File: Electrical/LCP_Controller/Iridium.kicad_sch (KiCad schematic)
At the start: 5 parts, among them J13 SALEAE_TEST, J14 U.FL, U14 IRIDIUM_9603N

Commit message: Hardware Revision : v0.3
1. modified schematic design, removed unnecessary test points.
2. pcb layout 2x8 Inches allowance dimension, layout is in progress
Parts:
- removed TP54: 5000, TestPoint:TestPoint_Keystone_5000-5004_Miniature, symbol Connector:TestPoint
- removed TP55: 5001, TestPoint:TestPoint_Keystone_5000-5004_Miniature, symbol Connector:TestPoint
- renumbered J13 to J5, J14 to J6, U14 to U5
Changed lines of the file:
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@@
-    (stroke (width 0) (type default) (color 0 0 0 0))
-  )
-  (wire (pts (xy 187.96 83.82) (xy 187.96 85.09))
     (stroke (width 0) (type default) (color 0 0 0 0))
   )
@@
   )
   (wire (pts (xy 161.29 123.19) (xy 161.29 125.73))
-    (stroke (width 0) (type default) (color 0 0 0 0))
-  )
-  (wire (pts (xy 163.83 83.82) (xy 163.83 86.36))
     (stroke (width 0) (type default) (color 0 0 0 0))
   )
@@
     (effects (font (size 1.27 1.27)) (justify right))
   )
-  (symbol (lib_id "Connector:TestPoint") (at 163.83 83.82 0) (unit 1)
-    (in_bom yes) (on_board yes)
-    (property "Reference" "TP54" (id 0) (at 165.3032 79.6798 0)
-      (effects (font (size 1.27 1.27)) (justify left))
-    )
-    (property "Value" "5000" (id 1) (at 165.3032 81.9912 0)
-      (effects (font (size 1.27 1.27)) (justify left))
-    )
-    (property "Footprint" "TestPoint:TestPoint_Keystone_5000-5004_Miniature" (id 2) (at 168.91 83.82 0)
-      (effects (font (size 1.27 1.27)) hide)
-    )
-    (property "Datasheet" "~" (id 3) (at 168.91 83.82 0)
-      (effects (font (size 1.27 1.27)) hide)
-    )
-    (property "TestPoint" "EXT_PWR" (id 4) (at 165.3032 84.3026 0)
-      (effects (font (size 1.27 1.27)) (justify left) hide)
-    )
-    (property "MPN" "" (id 5) (at 163.83 83.82 0)
-      (effects (font (size 1.27 1.27)) hide)
-    )
-    (pin "1")
-  )
-  (symbol (lib_id "Connector:TestPoint") (at 187.96 83.82 0) (unit 1)
-    (in_bom yes) (on_board yes)
-    (property "Reference" "TP55" (id 0) (at 189.4332 80.8228 0)
-      (effects (font (size 1.27 1.27)) (justify left))
-    )
-    (property "Value" "5001" (id 1) (at 189.4332 83.1342 0)
-      (effects (font (size 1.27 1.27)) (justify left))
-    )
-    (property "Footprint" "TestPoint:TestPoint_Keystone_5000-5004_Miniature" (id 2) (at 193.04 83.82 0)
-      (effects (font (size 1.27 1.27)) hide)
-    )
-    (property "Datasheet" "~" (id 3) (at 193.04 83.82 0)
-      (effects (font (size 1.27 1.27)) hide)
-    )
-    (property "TestPoint" "GND" (id 4) (at 187.96 83.82 0)
-      (effects (font (size 1.27 1.27)) hide)
-    )
-    (property "MPN" "" (id 5) (at 187.96 83.82 0)
-      (effects (font (size 1.27 1.27)) hide)
-    )
-    (pin "1")
-  )
-  (symbol (lib_id "power:GND") (at 187.96 85.09 0) (unit 1)
-    (in_bom yes) (on_board yes)
-    (property "Reference" "#PWR0125" (id 0) (at 187.96 91.44 0)
-      (effects (font (size 1.27 1.27)) hide)
-    )
-    (property "Value" "GND" (id 1) (at 188.087 89.4842 0))
-    (property "Footprint" "" (id 2) (at 187.96 85.09 0)
-      (effects (font (size 1.27 1.27)) hide)
-    )
-    (property "Datasheet" "" (id 3) (at 187.96 85.09 0)
-      (effects (font (size 1.27 1.27)) hide)
-    )
-    (pin "1")
-  )
   (symbol (lib_id "power:GND") (at 166.37 127 0) (unit 1)
     (in_bom yes) (on_board yes)
-    (property "Reference" "#PWR081" (id 0) (at 166.37 133.35 0)
+    (property "Reference" "#PWR047" (id 0) (at 166.37 133.35 0)
       (effects (font (size 1.27 1.27)) hide)
     )
@@
   (symbol (lib_id "Connector_Generic:Conn_02x04_Odd_Even") (at 129.54 81.28 90) (unit 1)
     (in_bom yes) (on_board yes)
-    (property "Reference" "J13" (id 0) (at 137.16 77.47 90)
+    (property "Reference" "J5" (id 0) (at 137.16 77.47 90)
       (effects (font (size 1.27 1.27)) (justify right))
     )
@@
   (symbol (lib_id "power:GND") (at 119.38 77.47 0) (unit 1)
     (in_bom yes) (on_board yes)
-    (property "Reference" "#PWR079" (id 0) (at 119.38 83.82 0)
+    (property "Reference" "#PWR044" (id 0) (at 119.38 83.82 0)
       (effects (font (size 1.27 1.27)) hide)
     )
@@
   (symbol (lib_id "power:GND") (at 139.7 118.11 0) (unit 1)
     (in_bom yes) (on_board yes)
-    (property "Reference" "#PWR080" (id 0) (at 139.7 124.46 0)
+    (property "Reference" "#PWR046" (id 0) (at 139.7 124.46 0)
       (effects (font (size 1.27 1.27)) hide)
     )
@@
   (symbol (lib_id "PMEL_RF:IRIDIUM_9603N") (at 166.37 91.44 0) (unit 1)
     (in_bom yes) (on_board yes)
-    (property "Reference" "U14" (id 0) (at 179.07 90.17 0))
+    (property "Reference" "U5" (id 0) (at 179.07 90.17 0))
     (property "Value" "IRIDIUM_9603N" (id 1) (at 154.94 90.17 0))
     (property "Footprint" "PMEL_Modules:Iridium_9603n" (id 2) (at 166.37 91.44 0)
@@
   (symbol (lib_id "Connector:Conn_Coaxial") (at 204.47 95.25 0) (mirror y) (unit 1)
     (in_bom yes) (on_board yes)
-    (property "Reference" "J14" (id 0) (at 201.93 95.885 0)
+    (property "Reference" "J6" (id 0) (at 201.93 95.885 0)
       (effects (font (size 1.27 1.27)) (justify left))
     )
@@
   (symbol (lib_id "power:GND") (at 204.47 105.41 0) (unit 1)
     (in_bom yes) (on_board yes)
-    (property "Reference" "#PWR082" (id 0) (at 204.47 111.76 0)
-      (effects (font (size 1.27 1.27)) hide)
-    )
+    (property "Reference" "#PWR045" (id 0) (at 204.47 111.76 0)
+      (effects (font (size 1.27 1.27)) hide)
+    )

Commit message: Hw Rev : 0.3v
changed buck-coverter LMR50410XDBVR to BD9G102G-LB, added schotty diode.
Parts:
- J6: value U.FL -> Conn_Coaxial
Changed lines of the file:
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@@
       (effects (font (size 1.27 1.27)) (justify left))
     )
-    (property "Value" "U.FL" (id 1) (at 201.93 98.1964 0)
-      (effects (font (size 1.27 1.27)) (justify left))
+    (property "Value" "Conn_Coaxial" (id 1) (at 201.93 98.1964 0)
+      (effects (font (size 1.27 1.27)) (justify left) hide)
     )
     (property "Footprint" "Connector_Coaxial:U.FL_Hirose_U.FL-R-SMT-1_Vertical" (id 2) (at 204.47 95.25 0)

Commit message: Connector Progress
J2 J22 and J23 converted to Molex Microfit

SALEAE TEST connectors removed
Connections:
- net GND: now also U5.14 (DTR)
- no-connect marks 5 -> 4
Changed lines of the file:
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@@
   (junction (at 127 95.25) (diameter 0) (color 0 0 0 0)
+  )
+  (junction (at 171.45 125.73) (diameter 0) (color 0 0 0 0)
   )
   (junction (at 129.54 97.79) (diameter 0) (color 0 0 0 0)
@@
   (no_connect (at 147.32 102.87))
   (no_connect (at 182.88 101.6))
-  (no_connect (at 182.88 104.14))
   (wire (pts (xy 154.94 86.36) (xy 163.83 86.36))
     (stroke (width 0) (type default))
@@
     (stroke (width 0) (type default))
   )
+  (wire (pts (xy 182.88 104.14) (xy 186.69 104.14))
+    (stroke (width 0) (type default))
+  )
   (wire (pts (xy 139.7 118.11) (xy 139.7 105.41))
     (stroke (width 0) (type default))
@@
   )
   (wire (pts (xy 102.87 97.79) (xy 129.54 97.79))
+    (stroke (width 0) (type default))
+  )
+  (wire (pts (xy 186.69 125.73) (xy 171.45 125.73))
     (stroke (width 0) (type default))
   )
@@
     (stroke (width 0) (type default))
   )
+  (wire (pts (xy 186.69 104.14) (xy 186.69 125.73))
+    (stroke (width 0) (type default))
+  )

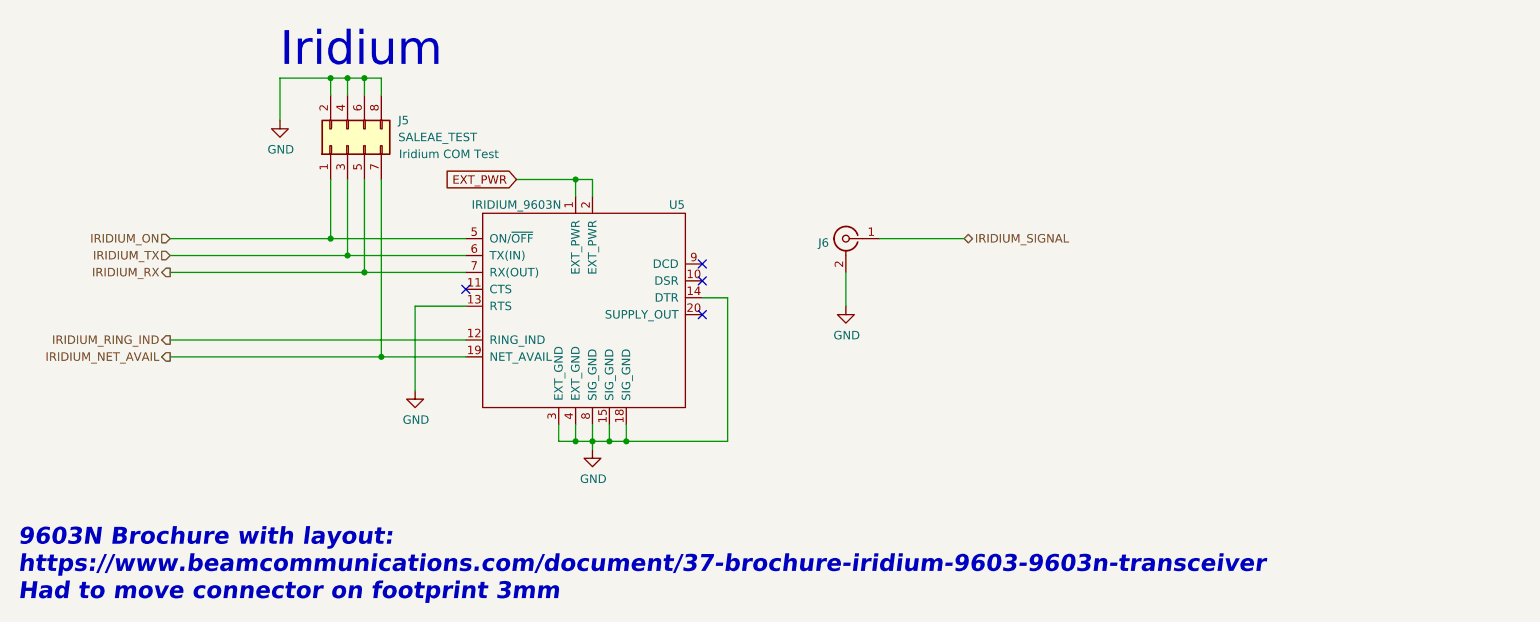
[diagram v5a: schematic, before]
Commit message: New Layout
Changes for this Rev:
- Impedance Matched GPS traces
- Copper Pours
- Vias/Traces changed to bring down costs
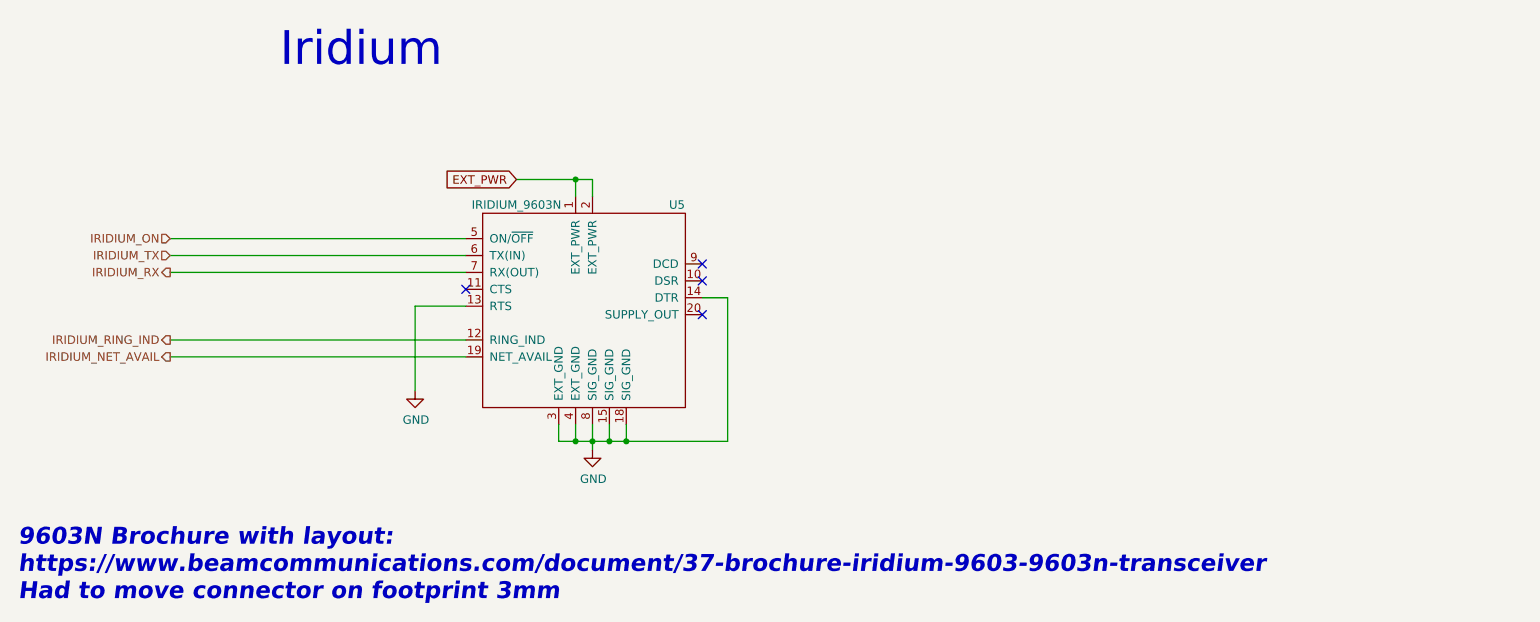
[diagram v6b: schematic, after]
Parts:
- removed J5: SALEAE_TEST, Connector_PinHeader_2.54mm:PinHeader_2x04_P2.54mm_Vertical, symbol Connector_Generic:Conn_02x04_Odd_Even
- removed J6: Conn_Coaxial, Connector_Coaxial:U.FL_Hirose_U.FL-R-SMT-1_Vertical, symbol Connector:Conn_Coaxial
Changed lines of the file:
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@@
     (comment 6 "Current Design Updated by: Joseph Kurina")
   )
-  (junction (at 127 71.12) (diameter 0) (color 0 0 0 0)
-  )
-  (junction (at 132.08 100.33) (diameter 0) (color 0 0 0 0)
-  )
-  (junction (at 129.54 71.12) (diameter 0) (color 0 0 0 0)
-  )
-  (junction (at 134.62 113.03) (diameter 0) (color 0 0 0 0)
-  )
   (junction (at 163.83 86.36) (diameter 0) (color 0 0 0 0)
   )
   (junction (at 168.91 125.73) (diameter 0) (color 0 0 0 0)
   )
-  (junction (at 132.08 71.12) (diameter 0) (color 0 0 0 0)
-  )
   (junction (at 163.83 125.73) (diameter 0) (color 0 0 0 0)
   )
-  (junction (at 127 95.25) (diameter 0) (color 0 0 0 0)
-  )
   (junction (at 171.45 125.73) (diameter 0) (color 0 0 0 0)
-  )
-  (junction (at 129.54 97.79) (diameter 0) (color 0 0 0 0)
   )
   (junction (at 166.37 125.73) (diameter 0) (color 0 0 0 0)
@@
     (stroke (width 0) (type default))
   )
-  (wire (pts (xy 127 73.66) (xy 127 71.12))
-    (stroke (width 0) (type default))
-  )
-  (wire (pts (xy 209.55 95.25) (xy 222.25 95.25))
-    (stroke (width 0) (type default))
-  )
   (wire (pts (xy 161.29 125.73) (xy 163.83 125.73))
     (stroke (width 0) (type default))
@@
     (stroke (width 0) (type default))
   )
-  (wire (pts (xy 127 86.36) (xy 127 95.25))
-    (stroke (width 0) (type default))
-  )
-  (wire (pts (xy 102.87 95.25) (xy 127 95.25))
-    (stroke (width 0) (type default))
-  )
   (wire (pts (xy 163.83 123.19) (xy 163.83 125.73))
     (stroke (width 0) (type default))
@@
     (stroke (width 0) (type default))
   )
-  (wire (pts (xy 129.54 86.36) (xy 129.54 97.79))
-    (stroke (width 0) (type default))
-  )
   (wire (pts (xy 182.88 104.14) (xy 186.69 104.14))
     (stroke (width 0) (type default))
@@
     (stroke (width 0) (type default))
   )
-  (wire (pts (xy 134.62 86.36) (xy 134.62 113.03))
-    (stroke (width 0) (type default))
-  )
-  (wire (pts (xy 102.87 97.79) (xy 129.54 97.79))
-    (stroke (width 0) (type default))
-  )
   (wire (pts (xy 186.69 125.73) (xy 171.45 125.73))
     (stroke (width 0) (type default))
   )
-  (wire (pts (xy 102.87 100.33) (xy 132.08 100.33))
-    (stroke (width 0) (type default))
-  )
-  (wire (pts (xy 129.54 71.12) (xy 132.08 71.12))
-    (stroke (width 0) (type default))
-  )
-  (wire (pts (xy 204.47 100.33) (xy 204.47 105.41))
-    (stroke (width 0) (type default))
-  )
   (wire (pts (xy 186.69 104.14) (xy 186.69 125.73))
     (stroke (width 0) (type default))
@@
     (stroke (width 0) (type default))
   )
-  (wire (pts (xy 132.08 73.66) (xy 132.08 71.12))
-    (stroke (width 0) (type default))
-  )
   (wire (pts (xy 168.91 125.73) (xy 166.37 125.73))
     (stroke (width 0) (type default))
   )
-  (wire (pts (xy 134.62 71.12) (xy 134.62 73.66))
-    (stroke (width 0) (type default))
-  )
   (wire (pts (xy 161.29 123.19) (xy 161.29 125.73))
     (stroke (width 0) (type default))
@@
     (stroke (width 0) (type default))
   )
-  (wire (pts (xy 132.08 71.12) (xy 134.62 71.12))
-    (stroke (width 0) (type default))
-  )
-  (wire (pts (xy 102.87 113.03) (xy 134.62 113.03))
-    (stroke (width 0) (type default))
-  )
   (wire (pts (xy 139.7 105.41) (xy 147.32 105.41))
     (stroke (width 0) (type default))
   )
-  (wire (pts (xy 132.08 86.36) (xy 132.08 100.33))
-    (stroke (width 0) (type default))
-  )
-  (wire (pts (xy 127 95.25) (xy 147.32 95.25))
-    (stroke (width 0) (type default))
-  )
-  (wire (pts (xy 147.32 100.33) (xy 132.08 100.33))
-    (stroke (width 0) (type default))
-  )
-  (wire (pts (xy 119.38 71.12) (xy 127 71.12))
-    (stroke (width 0) (type default))
-  )
-  (wire (pts (xy 129.54 73.66) (xy 129.54 71.12))
+  (wire (pts (xy 102.87 95.25) (xy 147.32 95.25))
+    (stroke (width 0) (type default))
+  )
+  (wire (pts (xy 102.87 100.33) (xy 147.32 100.33))
     (stroke (width 0) (type default))
   )
@@
     (stroke (width 0) (type default))
   )
-  (wire (pts (xy 127 71.12) (xy 129.54 71.12))
-    (stroke (width 0) (type default))
-  )
   (wire (pts (xy 171.45 125.73) (xy 168.91 125.73))
     (stroke (width 0) (type default))
   )
-  (wire (pts (xy 134.62 113.03) (xy 147.32 113.03))
-    (stroke (width 0) (type default))
-  )
-  (wire (pts (xy 129.54 97.79) (xy 147.32 97.79))
-    (stroke (width 0) (type default))
-  )
-  (wire (pts (xy 119.38 77.47) (xy 119.38 71.12))
+  (wire (pts (xy 102.87 113.03) (xy 147.32 113.03))
+    (stroke (width 0) (type default))
+  )
+  (wire (pts (xy 102.87 97.79) (xy 147.32 97.79))
     (stroke (width 0) (type default))
   )
@@
       (effects (font (size 1.27 1.27)) (justify right) hide)
     )
-  )
-  (hierarchical_label "IRIDIUM_SIGNAL" (shape bidirectional) (at 222.25 95.25 0) (fields_autoplaced)
-    (effects (font (size 1.27 1.27)) (justify left))
   )
   (hierarchical_label "IRIDIUM_RX" (shape output) (at 102.87 100.33 180) (fields_autoplaced)
@@
         (path "/df0f358a-57ab-4ee9-8b36-6ce64ef9d813/00000000-0000-0000-0000-00005eda42cc"
           (reference "#PWR047") (unit 1)
-        )
-      )
-    )
-  )
-  (symbol (lib_id "Connector_Generic:Conn_02x04_Odd_Even") (at 129.54 81.28 90) (unit 1)
-    (in_bom yes) (on_board yes) (dnp no)
-    (property "Reference" "J5" (at 137.16 77.47 90)
-      (effects (font (size 1.27 1.27)) (justify right))
-    )
-    (property "Value" "SALEAE_TEST" (at 137.16 80.01 90)
-      (effects (font (size 1.27 1.27)) (justify right))
-    )
-    (property "Footprint" "Connector_PinHeader_2.54mm:PinHeader_2x04_P2.54mm_Vertical" (at 129.54 81.28 0)
-      (effects (font (size 1.27 1.27)) hide)
-    )
-    (property "Datasheet" "~" (at 129.54 81.28 0)
-      (effects (font (size 1.27 1.27)) hide)
-    )
-    (property "TestPoint" "Iridium COM Test" (at 144.78 82.55 90)
-      (effects (font (size 1.27 1.27)))
-    )
-    (property "MPN" "0010897080" (at 129.54 81.28 0)
-      (effects (font (size 1.27 1.27)) hide)
-    )
-    (pin "1")
-    (pin "2")
-    (pin "3")
-    (pin "4")
-    (pin "5")
-    (pin "6")
-    (pin "7")
-    (pin "8")
-    (instances
-      (project "LCP_Controller"
-        (path "/df0f358a-57ab-4ee9-8b36-6ce64ef9d813/00000000-0000-0000-0000-00005eda42cc"
-          (reference "J5") (unit 1)
-        )
-      )
-    )
-  )
-  (symbol (lib_id "power:GND") (at 119.38 77.47 0) (unit 1)
-    (in_bom yes) (on_board yes) (dnp no)
-    (property "Reference" "#PWR044" (at 119.38 83.82 0)
-      (effects (font (size 1.27 1.27)) hide)
-    )
-    (property "Value" "GND" (at 119.507 81.8642 0)
-      (effects (font (size 1.27 1.27)))
-    )
-    (property "Footprint" "" (at 119.38 77.47 0)
-      (effects (font (size 1.27 1.27)) hide)
-    )
-    (property "Datasheet" "" (at 119.38 77.47 0)
-      (effects (font (size 1.27 1.27)) hide)
-    )
-    (pin "1")
-    (instances
-      (project "LCP_Controller"
-        (path "/df0f358a-57ab-4ee9-8b36-6ce64ef9d813/00000000-0000-0000-0000-00005eda42cc"
-          (reference "#PWR044") (unit 1)
         )
       )
@@
         )
       )
-    )
-  )
-  (symbol (lib_id "Connector:Conn_Coaxial") (at 204.47 95.25 0) (mirror y) (unit 1)
-    (in_bom yes) (on_board yes) (dnp no)
-    (property "Reference" "J6" (at 201.93 95.885 0)
-      (effects (font (size 1.27 1.27)) (justify left))
-    )
-    (property "Value" "Conn_Coaxial" (at 201.93 98.1964 0)
-      (effects (font (size 1.27 1.27)) (justify left) hide)
-    )
-    (property "Footprint" "Connector_Coaxial:U.FL_Hirose_U.FL-R-SMT-1_Vertical" (at 204.47 95.25 0)
-      (effects (font (size 1.27 1.27)) hide)
-    )
-    (property "Datasheet" " ~" (at 204.47 95.25 0)
-      (effects (font (size 1.27 1.27)) hide)
-    )
-    (property "MPN" "U.FL-R-SMT-1(10)" (at 204.47 95.25 0)
-      (effects (font (size 1.27 1.27)) hide)
-    )
-    (pin "1")
-    (pin "2")
-    (instances
-      (project "LCP_Controller"
-        (path "/df0f358a-57ab-4ee9-8b36-6ce64ef9d813/00000000-0000-0000-0000-00005eda42cc"
-          (reference "J6") (unit 1)
-        )
-      )
-    )
-  )
-  (symbol (lib_id "power:GND") (at 204.47 105.41 0) (unit 1)
-    (in_bom yes) (on_board yes) (dnp no)
-    (property "Reference" "#PWR045" (at 204.47 111.76 0)
-      (effects (font (size 1.27 1.27)) hide)
-    )
-    (property "Value" "GND" (at 204.597 109.8042 0)
-      (effects (font (size 1.27 1.27)))
-    )
-    (property "Footprint" "" (at 204.47 105.41 0)
-      (effects (font (size 1.27 1.27)) hide)
-    )
-    (property "Datasheet" "" (at 204.47 105.41 0)
-      (effects (font (size 1.27 1.27)) hide)
-    )
-    (pin "1")
-    (instances
-      (project "LCP_Controller"
-        (path "/df0f358a-57ab-4ee9-8b36-6ce64ef9d813/00000000-0000-0000-0000-00005eda42cc"
-          (reference "#PWR045") (unit 1)
-        )
-      )
